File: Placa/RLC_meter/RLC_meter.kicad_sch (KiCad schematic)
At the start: 10 parts, among them J1 Batt in, U1 LPC845, U3 L7805, U4 LM358

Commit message: massive update. Local to git
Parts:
- removed J?: Batt in, Battery:BatteryHolder_Keystone_2479_3xAAA, symbol Connector:Conn_01x02_Female
- removed R?: R, Resistor_THT:R_Axial_DIN0207_L6.3mm_D2.5mm_P10.16mm_Horizontal, symbol Device:R
- removed U1: LPC845, RLC_meter:LPC845, symbol RLC_meter:LPC845
- removed U3: L7805, Package_TO_SOT_THT:TO-220-3_Horizontal_TabDown, symbol Regulator_Linear:L7805
- removed U4: LM358, symbol Amplifier_Operational:LM358
- added C3, C4: 100n, Capacitor_THT:C_Disc_D5.0mm_W2.5mm_P2.50mm, symbol Device:C
- added C5: 100u, Capacitor_THT:CP_Radial_D8.0mm_P5.00mm, symbol Device:C_Polarized
- added J2: Batt2, Connector_PinHeader_2.54mm:PinHeader_1x02_P2.54mm_Vertical, symbol Connector:Conn_01x02_Female
- added J3: HC05, Connector_PinHeader_2.54mm:PinHeader_1x04_P2.54mm_Horizontal, symbol Connector:Conn_01x04_Female
- added J4: Load_terminal, TerminalBlock_Philmore:TerminalBlock_Philmore_TB132_1x02_P5.00mm_Horizontal, symbol Connector:Screw_Terminal_01x02
- added R3, R4: 100k, Resistor_THT:R_Axial_DIN0309_L9.0mm_D3.2mm_P15.24mm_Horizontal, symbol Device:R
- added R5, R6: 560, Resistor_THT:R_Axial_DIN0309_L9.0mm_D3.2mm_P15.24mm_Horizontal, symbol Device:R
- added RV1: 50k, Potentiometer_THT:Potentiometer_Bourns_3386C_Horizontal, symbol Device:R_Potentiometer_Trim
- added U1: LPC845, RLC_meter:LPC845, symbol proj_lib:LPC845
- added U2: X9Cxxx, Package_DIP:DIP-8_W7.62mm_Socket_LongPads, symbol Potentiometer_Digital:X9Cxxx
- added U3: MC33202, Package_DIP:DIP-8_W7.62mm_Socket_LongPads, symbol Amplifier_Operational:MC33202
- added U4: L7805, Package_TO_SOT_THT:TO-220-3_Horizontal_TabDown, symbol Regulator_Linear:L7805
- added U5: AMS1117-3.3, Connector_PinHeader_2.54mm:PinHeader_1x03_P2.54mm_Vertical, symbol Regulator_Linear:AMS1117-3.3
- C1, C2: value C -> 100n; footprint Capacitor_THT:C_Axial_L5.1mm_D3.1mm_P7.50mm_Horizontal -> Capacitor_THT:C_Disc_D5.0mm_W2.5mm_P2.50mm
- J1: value Batt in -> Batt1; footprint Battery:BatteryHolder_Keystone_2479_3xAAA -> Connector_PinHeader_2.54mm:PinHeader_1x02_P2.54mm_Vertical
- R1: value 100k -> 150k; footprint Resistor_THT:R_Axial_DIN0207_L6.3mm_D2.5mm_P10.16mm_Horizontal -> Resistor_THT:R_Axial_DIN0309_L9.0mm_D3.2mm_P15.24mm_Horizontal
- R2: value R -> 220k; footprint Resistor_THT:R_Axial_DIN0207_L6.3mm_D2.5mm_P10.16mm_Horizontal -> Resistor_THT:R_Axial_DIN0309_L9.0mm_D3.2mm_P15.24mm_Horizontal
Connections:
- net +BATT: now also C3.1, U3.8 (V+), U4.1 (IN); no longer C1.1
- net GND: now also C3.2, C4.2, C5.2, J2.1 (Pin_1), J3.2 (Pin_2), J4.2 (Pin_2), R6.1, RV1.3, U1.20 (GND), U2.4, U2.6 (VL), U3.3 (+), U4.2 (GND), U5.1 (GND)
- net Signal_i: now also R4.2, R5.1, U1.32 (PIO_07/ADC0), U3.1
- net at R1.2, R2.1: now also RV1.1
- net Signal_1 renamed -BATT
- net -BATT: now also J2.2 (Pin_2), U3.4 (V-)
- net VCC renamed +3.3V
- net +3.3V: now also U1.40 (VCC), U5.2 (VO)
- new net: R3.1, R4.1, RV1.2, U3.2 (-)
- new net +5V: C1.1, C4.1, C5.1, J3.1 (Pin_1), U2.8, U4.3 (OUT), U5.3 (VI)
- new net POT+: R6.2, U2.3 (VH), U3.6 (-)
- new net POT_CS: U1.28 (PIO_15), U2.7 (~{CS})
- new net POT_INC: U1.26 (PIO_13), U2.1 (~{INC})
- new net POT_U/D: U1.27 (PIO_14/ADC2), U2.2 (U/~{D})
- new net POT_V: U1.33 (PIO_06/ADC1), U2.5 (VW), U3.7
- new net RX: J3.3 (Pin_3), U1.11 (PIO_25)
- new net TX: J3.4 (Pin_4), U1.10 (PIO_24)
- new net V_DAC: R3.2, U1.2 (PIO_17/ADC9/DAC0)
- new net generated_signal: J4.1 (Pin_1), R5.2, U3.5 (+)
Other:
- note added: "+"
- moved on the sheet: C1, C2, J1

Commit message: correxiones en clase
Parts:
- R6: value 560 -> 33
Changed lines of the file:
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@@
       (effects (font (size 1.27 1.27)) (justify left))
     )
-    (property "Value" "560" (id 1) (at 97.79 97.79 90)
+    (property "Value" "33" (id 1) (at 97.79 97.79 90)
       (effects (font (size 1.27 1.27)) (justify left))
     )
@@
     )
     (path "/e1ec8ca0-d2aa-4a0d-b05b-78b7b8e4e859"
-      (reference "R6") (unit 1) (value "560") (footprint "Resistor_THT:R_Axial_DIN0309_L9.0mm_D3.2mm_P15.24mm_Horizontal")
+      (reference "R6") (unit 1) (value "33") (footprint "Resistor_THT:R_Axial_DIN0309_L9.0mm_D3.2mm_P15.24mm_Horizontal")
     )
     (path "/8043014b-f53c-43be-b39f-70fd6c5f044a"

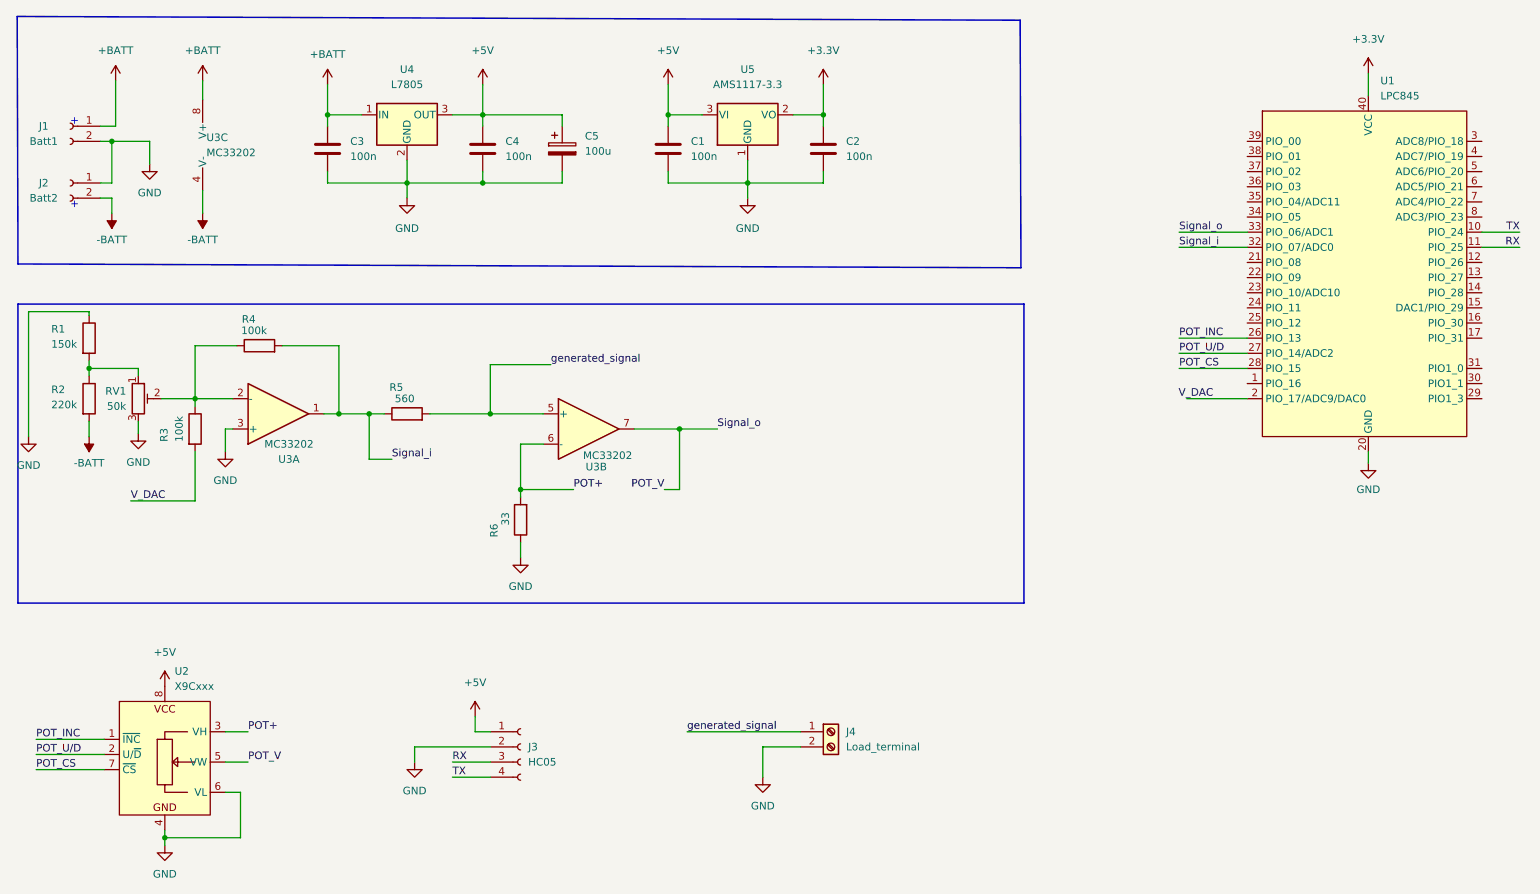
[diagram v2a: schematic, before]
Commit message: fixed frecuency, single letter command, general revision
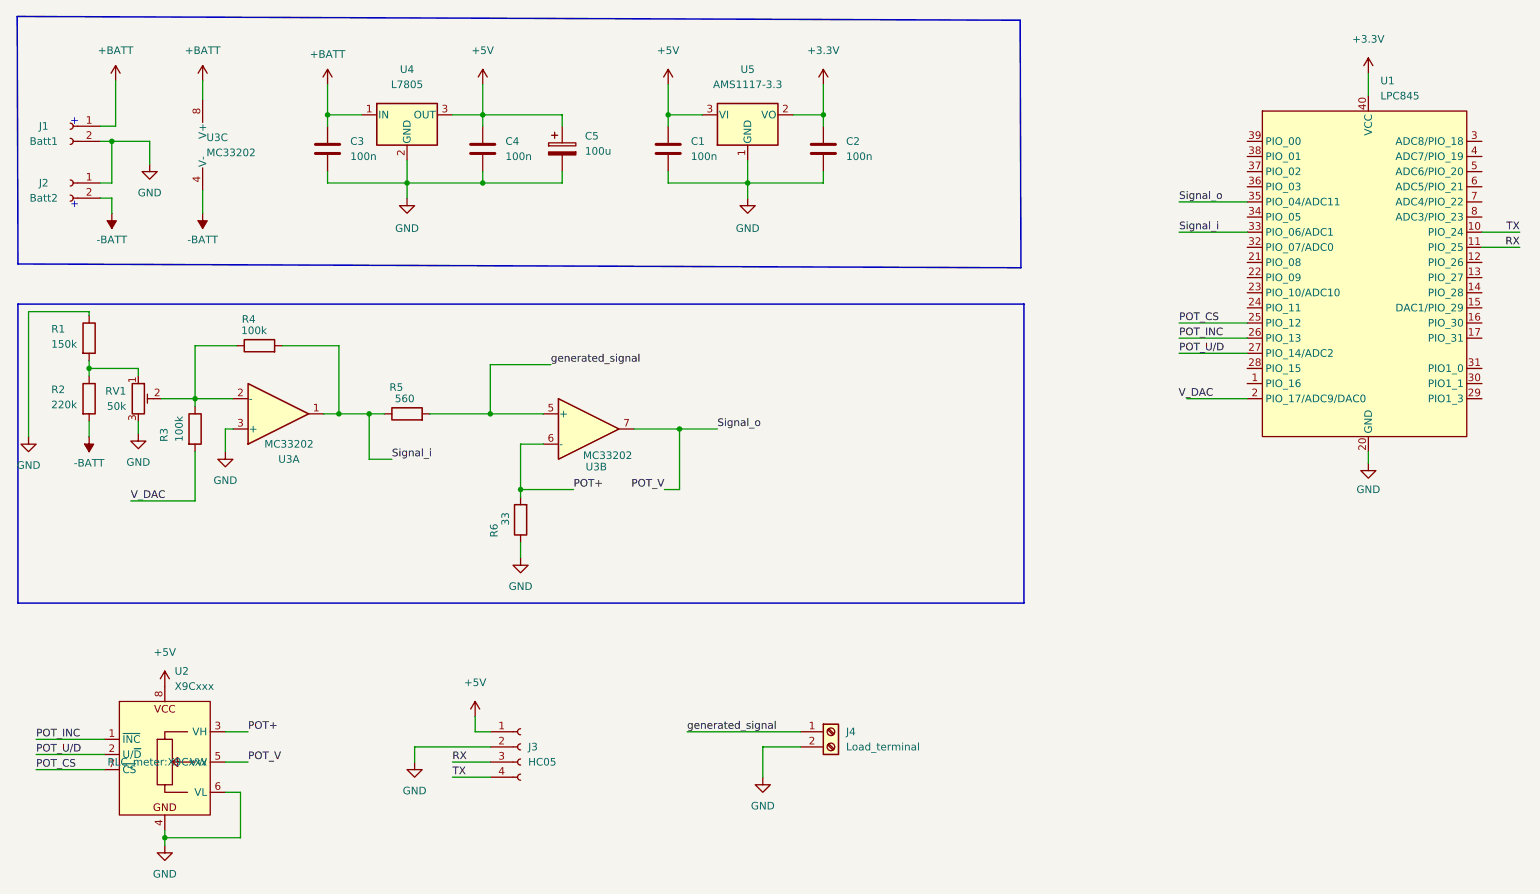
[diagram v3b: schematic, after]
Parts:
- R1, R2, R3, R4, R5, R6: footprint Resistor_THT:R_Axial_DIN0309_L9.0mm_D3.2mm_P15.24mm_Horizontal -> Resistor_THT:R_Axial_DIN0207_L6.3mm_D2.5mm_P15.24mm_Horizontal
- U2: footprint Package_DIP:DIP-8_W7.62mm_Socket_LongPads -> RLC_meter:X9Cxxx
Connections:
- net POT_CS: now also U1.25 (PIO_12); no longer U1.28 (PIO_15)
- net POT_V: now also U1.35 (PIO_04/ADC11); no longer U1.33 (PIO_06/ADC1)
- net Signal_i: now also U1.33 (PIO_06/ADC1); no longer U1.32 (PIO_07/ADC0)
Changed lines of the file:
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@@
+    (stroke (width 0) (type default) (color 0 0 0 0))
+  )
+  (wire (pts (xy 210.82 50.8) (xy 222.25 50.8))
     (stroke (width 0) (type default) (color 0 0 0 0))
   )
@@
     (stroke (width 0) (type default) (color 0 0 0 0))
   )
-  (wire (pts (xy 210.82 53.34) (xy 222.25 53.34))
+  (wire (pts (xy 210.82 45.72) (xy 222.25 45.72))
     (stroke (width 0) (type default) (color 0 0 0 0))
   )
@@
   )
   (wire (pts (xy 140.97 142.24) (xy 140.97 137.16))
-    (stroke (width 0) (type default) (color 0 0 0 0))
-  )
-  (wire (pts (xy 210.82 73.66) (xy 222.25 73.66))
     (stroke (width 0) (type default) (color 0 0 0 0))
   )
@@
     (stroke (width 0) (type default) (color 0 0 0 0))
   )
+  (wire (pts (xy 210.82 66.04) (xy 222.25 66.04))
+    (stroke (width 0) (type default) (color 0 0 0 0))
+  )
   (wire (pts (xy 125.095 40.64) (xy 125.095 42.545))
     (stroke (width 0) (type default) (color 0 0 0 0))
@@
   )
   (wire (pts (xy 46.99 43.815) (xy 46.99 47.625))
-    (stroke (width 0) (type default) (color 0 0 0 0))
-  )
-  (wire (pts (xy 210.82 50.8) (xy 222.25 50.8))
     (stroke (width 0) (type default) (color 0 0 0 0))
   )
@@
     (effects (font (size 1.27 1.27)) (justify left bottom))
   )
-  (label "Signal_o" (at 210.82 50.8 0)
-    (effects (font (size 1.27 1.27)) (justify left bottom))
-  )
   (label "POT_INC" (at 210.82 68.58 0)
+    (effects (font (size 1.27 1.27)) (justify left bottom))
+  )
+  (label "Signal_i" (at 210.82 50.8 0)
     (effects (font (size 1.27 1.27)) (justify left bottom))
   )
@@
     (effects (font (size 1.27 1.27)) (justify left bottom))
   )
-  (label "POT_CS" (at 210.82 73.66 0)
-    (effects (font (size 1.27 1.27)) (justify left bottom))
-  )
   (label "TX" (at 267.97 50.8 180)
     (effects (font (size 1.27 1.27)) (justify right bottom))
   )
+  (label "POT_CS" (at 210.82 66.04 0)
+    (effects (font (size 1.27 1.27)) (justify left bottom))
+  )
   (label "RX" (at 267.97 53.34 180)
     (effects (font (size 1.27 1.27)) (justify right bottom))
@@
     (effects (font (size 1.27 1.27)) (justify left bottom))
   )
+  (label "Signal_o" (at 210.82 45.72 0)
+    (effects (font (size 1.27 1.27)) (justify left bottom))
+  )
   (label "TX" (at 88.9 142.24 0)
     (effects (font (size 1.27 1.27)) (justify left bottom))
   )
   (label "POT+" (at 109.22 93.98 0)
-    (effects (font (size 1.27 1.27)) (justify left bottom))
-  )
-  (label "Signal_i" (at 210.82 53.34 0)
     (effects (font (size 1.27 1.27)) (justify left bottom))
   )
@@
       (effects (font (size 1.27 1.27)) (justify left))
     )
-    (property "Footprint" "Resistor_THT:R_Axial_DIN0309_L9.0mm_D3.2mm_P15.24mm_Horizontal" (id 2) (at 26.162 68.58 90)
+    (property "Footprint" "Resistor_THT:R_Axial_DIN0207_L6.3mm_D2.5mm_P15.24mm_Horizontal" (id 2) (at 26.162 68.58 90)
       (effects (font (size 1.27 1.27)) hide)
     )
@@
       (effects (font (size 1.27 1.27)) (justify left))
     )
-    (property "Footprint" "Resistor_THT:R_Axial_DIN0309_L9.0mm_D3.2mm_P15.24mm_Horizontal" (id 2) (at 81.28 83.058 90)
+    (property "Footprint" "Resistor_THT:R_Axial_DIN0207_L6.3mm_D2.5mm_P15.24mm_Horizontal" (id 2) (at 81.28 83.058 90)
       (effects (font (size 1.27 1.27)) hide)
     )
@@
       (effects (font (size 1.27 1.27)) (justify left))
     )
-    (property "Footprint" "Resistor_THT:R_Axial_DIN0309_L9.0mm_D3.2mm_P15.24mm_Horizontal" (id 2) (at 43.942 83.82 90)
+    (property "Footprint" "Resistor_THT:R_Axial_DIN0207_L6.3mm_D2.5mm_P15.24mm_Horizontal" (id 2) (at 43.942 83.82 90)
       (effects (font (size 1.27 1.27)) hide)
     )
@@
       (effects (font (size 1.27 1.27)) (justify left))
     )
-    (property "Footprint" "Resistor_THT:R_Axial_DIN0309_L9.0mm_D3.2mm_P15.24mm_Horizontal" (id 2) (at 56.515 71.628 90)
+    (property "Footprint" "Resistor_THT:R_Axial_DIN0207_L6.3mm_D2.5mm_P15.24mm_Horizontal" (id 2) (at 56.515 71.628 90)
       (effects (font (size 1.27 1.27)) hide)
     )
@@
       (effects (font (size 1.27 1.27)) (justify left))
     )
-    (property "Footprint" "Resistor_THT:R_Axial_DIN0309_L9.0mm_D3.2mm_P15.24mm_Horizontal" (id 2) (at 26.162 78.74 90)
+    (property "Footprint" "Resistor_THT:R_Axial_DIN0207_L6.3mm_D2.5mm_P15.24mm_Horizontal" (id 2) (at 26.162 78.74 90)
       (effects (font (size 1.27 1.27)) hide)
     )
@@
       (effects (font (size 1.27 1.27)) (justify left))
     )
-    (property "Footprint" "Resistor_THT:R_Axial_DIN0309_L9.0mm_D3.2mm_P15.24mm_Horizontal" (id 2) (at 102.108 99.06 90)
+    (property "Footprint" "Resistor_THT:R_Axial_DIN0207_L6.3mm_D2.5mm_P15.24mm_Horizontal" (id 2) (at 102.108 99.06 90)
       (effects (font (size 1.27 1.27)) hide)
     )
@@
       (effects (font (size 1.27 1.27)) (justify left))
     )
-    (property "Footprint" "Package_DIP:DIP-8_W7.62mm_Socket_LongPads" (id 2) (at 39.37 139.7 0)
-      (effects (font (size 1.27 1.27)) hide)
-    )
+    (property "Footprint" "RLC_meter:X9Cxxx" (id 2) (at 39.37 139.7 0))
     (property "Datasheet" "" (id 3) (at 39.37 139.7 0)
       (effects (font (size 1.27 1.27)) hide)
@@
     )
     (path "/0e8f76f9-df88-4206-b4bd-8d5f827c78fc"
-      (reference "R1") (unit 1) (value "150k") (footprint "Resistor_THT:R_Axial_DIN0309_L9.0mm_D3.2mm_P15.24mm_Horizontal")
+      (reference "R1") (unit 1) (value "150k") (footprint "Resistor_THT:R_Axial_DIN0207_L6.3mm_D2.5mm_P15.24mm_Horizontal")
     )
     (path "/be6c2d9a-8927-4d50-9ea7-a02e5e31d462"
-      (reference "R2") (unit 1) (value "220k") (footprint "Resistor_THT:R_Axial_DIN0309_L9.0mm_D3.2mm_P15.24mm_Horizontal")
+      (reference "R2") (unit 1) (value "220k") (footprint "Resistor_THT:R_Axial_DIN0207_L6.3mm_D2.5mm_P15.24mm_Horizontal")
     )
     (path "/64e825e4-9bb4-4e3b-b28b-6f7b09737104"
-      (reference "R3") (unit 1) (value "100k") (footprint "Resistor_THT:R_Axial_DIN0309_L9.0mm_D3.2mm_P15.24mm_Horizontal")
+      (reference "R3") (unit 1) (value "100k") (footprint "Resistor_THT:R_Axial_DIN0207_L6.3mm_D2.5mm_P15.24mm_Horizontal")
     )
     (path "/b8feebea-7122-4a58-8789-f22c93ffa637"
-      (reference "R4") (unit 1) (value "100k") (footprint "Resistor_THT:R_Axial_DIN0309_L9.0mm_D3.2mm_P15.24mm_Horizontal")
+      (reference "R4") (unit 1) (value "100k") (footprint "Resistor_THT:R_Axial_DIN0207_L6.3mm_D2.5mm_P15.24mm_Horizontal")
     )
     (path "/424aa96b-31c6-47e4-bd05-9dd963300f77"
-      (reference "R5") (unit 1) (value "560") (footprint "Resistor_THT:R_Axial_DIN0309_L9.0mm_D3.2mm_P15.24mm_Horizontal")
+      (reference "R5") (unit 1) (value "560") (footprint "Resistor_THT:R_Axial_DIN0207_L6.3mm_D2.5mm_P15.24mm_Horizontal")
     )
     (path "/e1ec8ca0-d2aa-4a0d-b05b-78b7b8e4e859"
-      (reference "R6") (unit 1) (value "33") (footprint "Resistor_THT:R_Axial_DIN0309_L9.0mm_D3.2mm_P15.24mm_Horizontal")
+      (reference "R6") (unit 1) (value "33") (footprint "Resistor_THT:R_Axial_DIN0207_L6.3mm_D2.5mm_P15.24mm_Horizontal")
     )
     (path "/8043014b-f53c-43be-b39f-70fd6c5f044a"
@@
     )
     (path "/eaa38b37-d929-4066-aca8-4e66d295820a"
-      (reference "U2") (unit 1) (value "X9Cxxx") (footprint "Package_DIP:DIP-8_W7.62mm_Socket_LongPads")
+      (reference "U2") (unit 1) (value "X9Cxxx") (footprint "RLC_meter:X9Cxxx")
     )
     (path "/c74730c4-8724-4e1b-a5d7-b267f7209836"

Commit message: last commit
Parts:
- R1: value 150k -> 100k
- R2: value 220k -> 10k
- R5: value 560 -> 470
- RV1: value 50k -> 10k
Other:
- moved on the sheet: J3, J4, R1, R2, R3, R4, R5, R6, RV1, U1, U2, U3A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
